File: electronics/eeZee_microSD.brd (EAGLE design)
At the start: 18.3 x 29.8 mm, 14 parts, among them U1 MCP1824S, U2 74HC4050, U3 USD-SOCKET

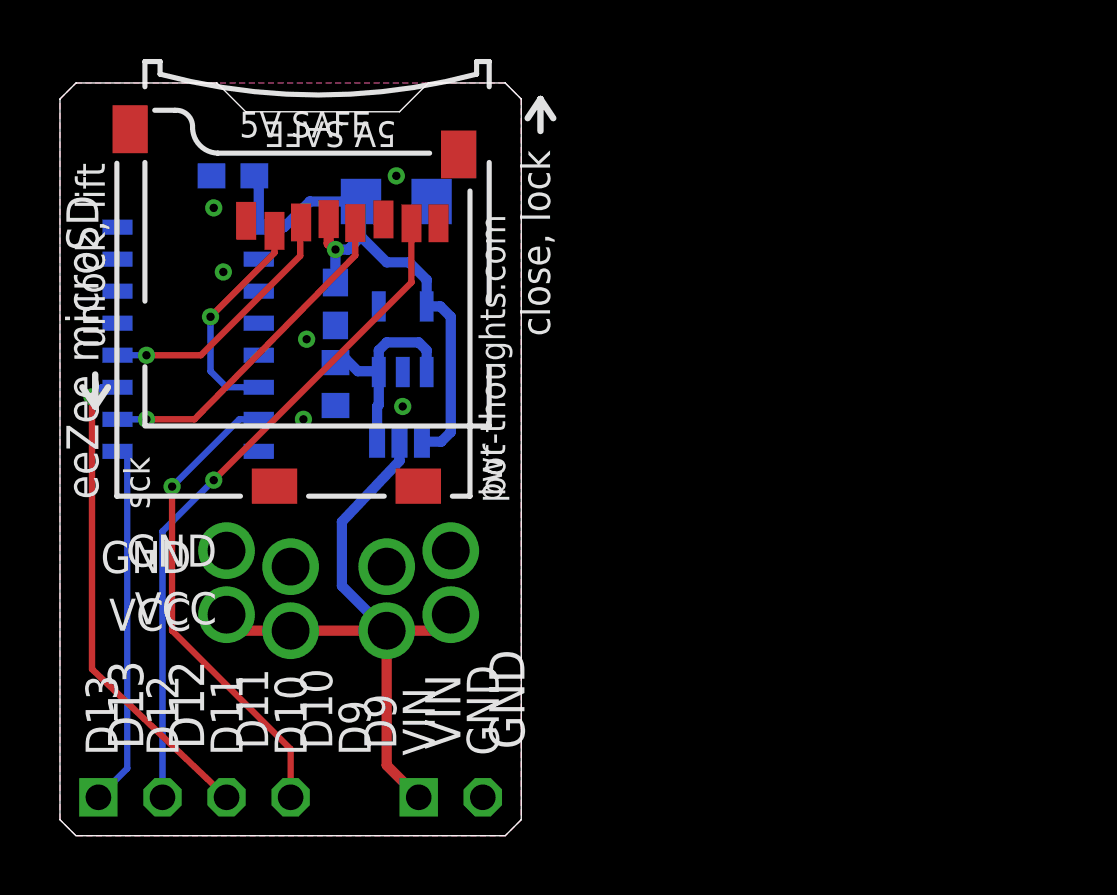
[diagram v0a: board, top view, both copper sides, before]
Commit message: modified silk layout
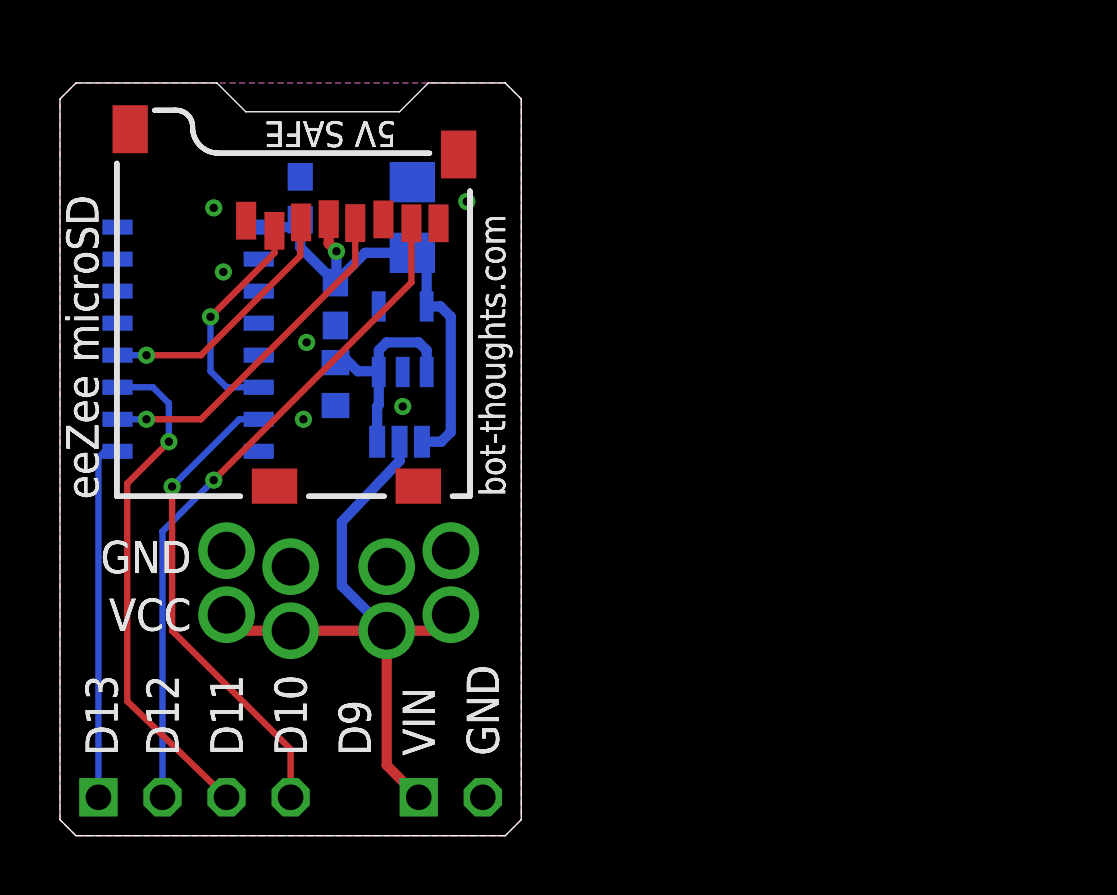
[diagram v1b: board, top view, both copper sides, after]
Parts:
- moved C2 2.81 mm to (9.53, 25.3), turned to 90 degrees
- moved C1 0.90 mm to (14.0, 24.5), turned to 90 degrees
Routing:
- net VCC: track 23.4 -> 20.4 mm
- net MOSI_HV: track 19.3 -> 20.3 mm
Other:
- board text added: "104"
- board text added: "106"
- board text added: "10K"
- board text added: "74HC4050"
- board text added: "MCP1824S"
- board text removed: "C1"
- board text removed: "C2"
- board text removed: "C3"
- board text removed: "R0.2"
- board text removed: "R5"
- board text removed: "U1"
- board text removed: "U2"
- board text removed: "close, lock"
- board text removed: "pwr"
- board text removed: "sck"
- board text removed: "unlock, lift"

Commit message: Updated schematic version and usd socket value
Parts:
- U3: value USD-SOCKET -> USD-PUSHPULL
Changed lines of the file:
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@@
 <attribute name="DATABASE" value="./../../../eagle/PARTSDB.TXT" x="12.954" y="8.128" size="1.778" layer="28" rot="MR90" display="off"/>
 </element>
-<element name="U3" library="SparkFun-Connectors" package="MICROSD_1:1" value="USD-SOCKET" x="2.286" y="13.462" smashed="yes">
+<element name="U3" library="SparkFun-Connectors" package="MICROSD_1:1" value="USD-PUSHPULL" x="2.286" y="13.462" smashed="yes">
 <attribute name="PROD_ID" value="CONN-07820" x="2.286" y="13.462" size="1.778" layer="27" display="off"/>
 </element>

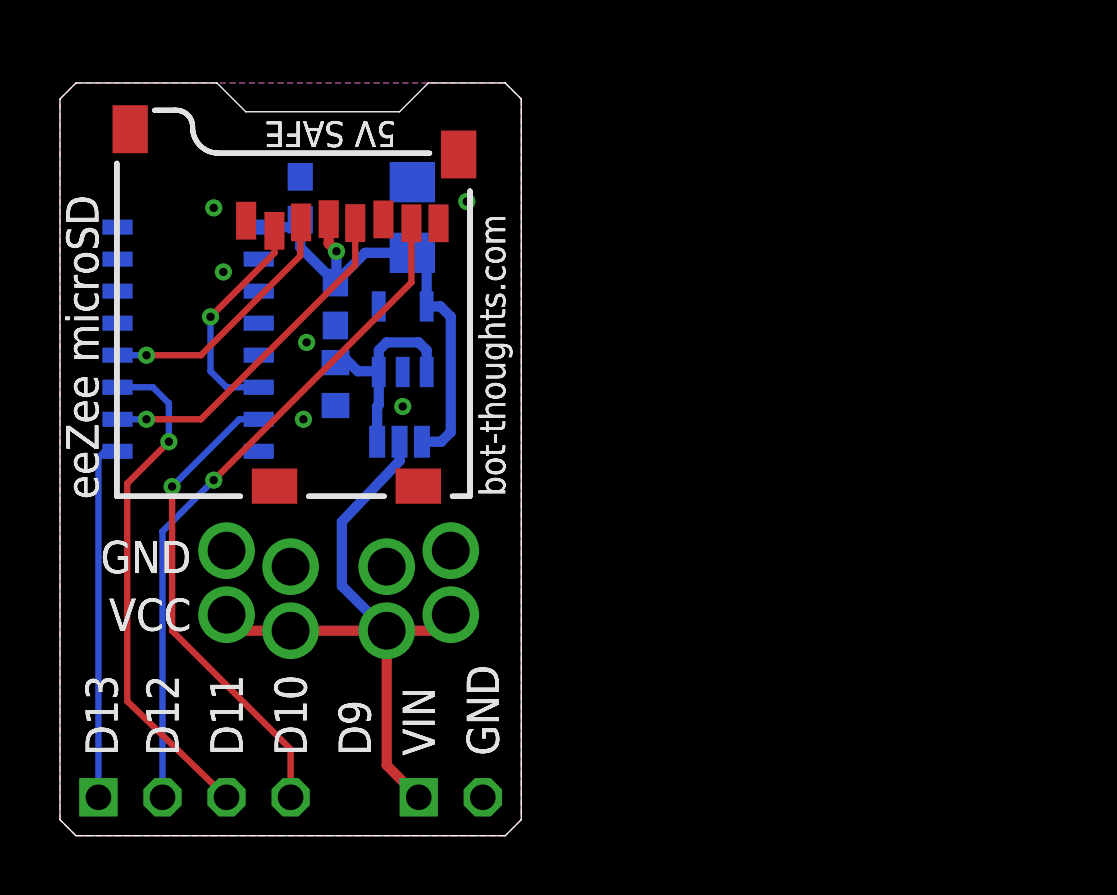
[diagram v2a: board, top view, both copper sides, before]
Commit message: Updated version with flip-top socket
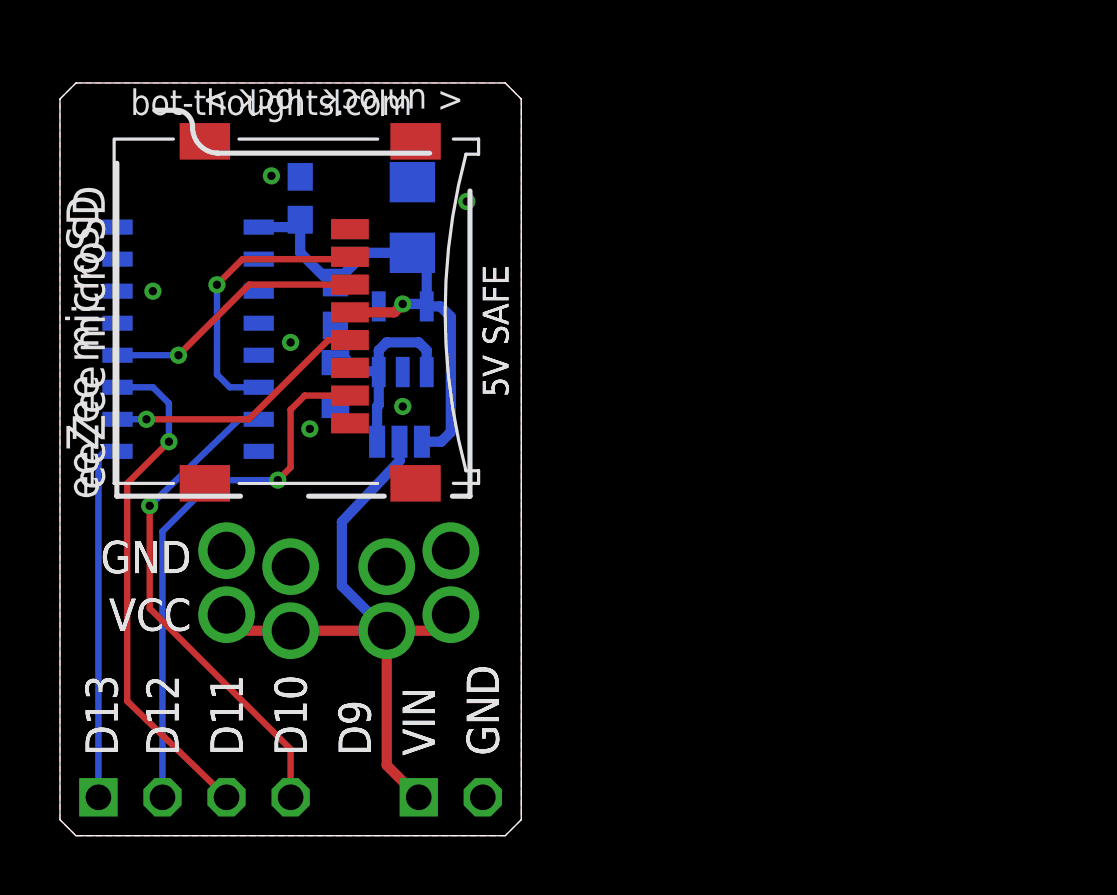
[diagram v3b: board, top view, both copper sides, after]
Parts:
- removed U3: USD-PUSHPULL, SparkFun-Connectors:MICROSD_1:1
- added U$1: MICROSD_TFLASH, bt_electromech:TFLASH_CP-0000-086
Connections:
- net !SS: now also U$1.CS; no longer U3.2
- net GND: now also U$1.GND, U$1.SHIELD1, U$1.SHIELD2, U$1.SHIELD3, U$1.SHIELD4; no longer U3.6, U3.CD1, U3.CD2, U3.GND1, U3.GND3
- net MISO: now also U$1.DO; no longer U3.7
- net MOSI: now also U$1.DI; no longer U3.3
- net SCK: now also U$1.SCLK; no longer U3.5
- net VCC: now also U$1.VDD; no longer U3.4
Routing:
- net MISO: track 26.8 -> 21.5 mm
- net SCK: track 13.6 -> 10.5 mm
- net !SS: track 8.79 -> 11.2 mm
- net !CS_HV: track 18.8 -> 19.6 mm
- net VCC: track 20.4 -> 21.1 mm
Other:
- outline, holes or cut-outs redrawn
- board text added: "< unlock lock >"
- board text added: "R0.3B"

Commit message: Used small manual connector. Total layout redesign, shrunk board considerably, removed power rail pin headers
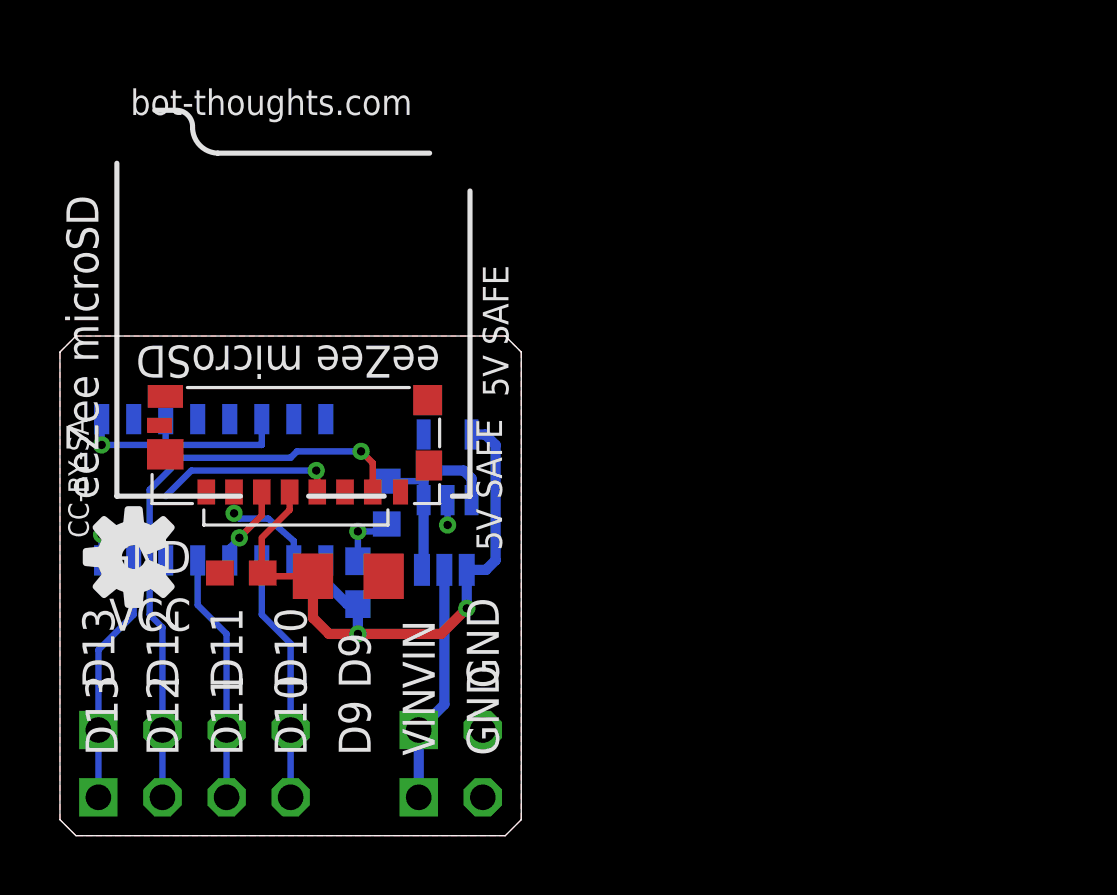
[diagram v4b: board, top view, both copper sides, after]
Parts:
- removed JP4, JP5: PWR, mes_electromech:BIGPIN-2
- removed U$1: MICROSD_TFLASH, bt_electromech:TFLASH_CP-0000-086
- added U3: MICROSD_SMALL, bt_electromech:USD_SMALL
- JP1: value (none) -> PWR
- JP2: value PWR -> (none); device mes_electromech:BIGPIN-2 -> pinhead-2:1X04-S
- JP3: device mes_electromech:BIGPIN-2 -> pinhead-2:1X02-S
- moved C2 15.4 mm to (11.8, 10.0)
- moved C1 14.4 mm to (11.4, 10.3), flipped to the top, turned to 0 degrees
- moved JP2 12.5 mm to (5.33, 1.52), turned to 180 degrees
- moved C3 11.3 mm to (7.19, 10.4), flipped to the top, turned to 180 degrees
- moved JP3 9.16 mm to (15.5, 1.52), turned to 180 degrees
- moved U2 6.05 mm to (6.10, 13.7), turned to 0 degrees
- moved REG 5.38 mm to (15.2, 10.5)
- moved U1 5.38 mm to (15.4, 14.6)
- moved R5 5.12 mm to (13.0, 13.2)
- moved JP1 2.67 mm to (15.5, 4.19)
- moved JP6 2.67 mm to (5.33, 4.19)
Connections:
- removed net VBOARD: JP1.1, JP2.P$1, JP3.P$1, JP4.P$1, JP5.P$1, REG.2
- new net VIN: JP1.1, JP3.1, REG.2
- net !CS_HV: now also JP2.4, U2.3; no longer U2.7
- net !SS: now also U2.2, U3.2; no longer U$1.CS, U2.6
- net GND: now also JP3.2, U2.11, U2.9, U3.6, U3.GND1, U3.GND2, U3.GND3, U3.GND4; no longer JP2.P$2, JP3.P$2, JP4.P$2, JP5.P$2, U$1.GND, U$1.SHIELD1, U$1.SHIELD2, U$1.SHIELD3, U$1.SHIELD4, U2.3, U2.5
- net MISO: now also JP2.2, U3.7; no longer U$1.DO
- net MOSI: now also U2.4, U3.3; no longer U$1.DI, U2.12
- net MOSI_HV: now also JP2.3, U2.5; no longer U2.11
- net SCK: now also U2.6, U3.5; no longer U$1.SCLK, U2.10
- net SCK_HV: now also JP2.1, U2.7; no longer U2.9
- net VCC: now also U3.4; no longer U$1.VDD
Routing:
- net VBOARD: track 25.7 -> 0.00 mm
- net GND: track 0.00 -> 13.9 mm, vias 6 -> 4
- net MOSI_HV: track 20.3 -> 10.0 mm, vias 1 -> 0
- net !CS_HV: track 19.6 -> 9.87 mm, vias 1 -> 0
- net VIN: track 0.00 -> 9.44 mm
- net !SS: track 11.2 -> 3.56 mm
- net MOSI: track 10.4 -> 3.24 mm
- net VCC: track 21.1 -> 26.4 mm, vias 1 -> 2
- net SCK_HV: track 14.7 -> 9.97 mm
- net SCK: track 10.5 -> 7.26 mm
- net MISO: track 21.5 -> 23.2 mm
- removed copper zone on layer 16, net GND
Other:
- board size 18.3 x 29.8 mm -> 18.3 x 19.8 mm
- board text removed: "< unlock lock >"

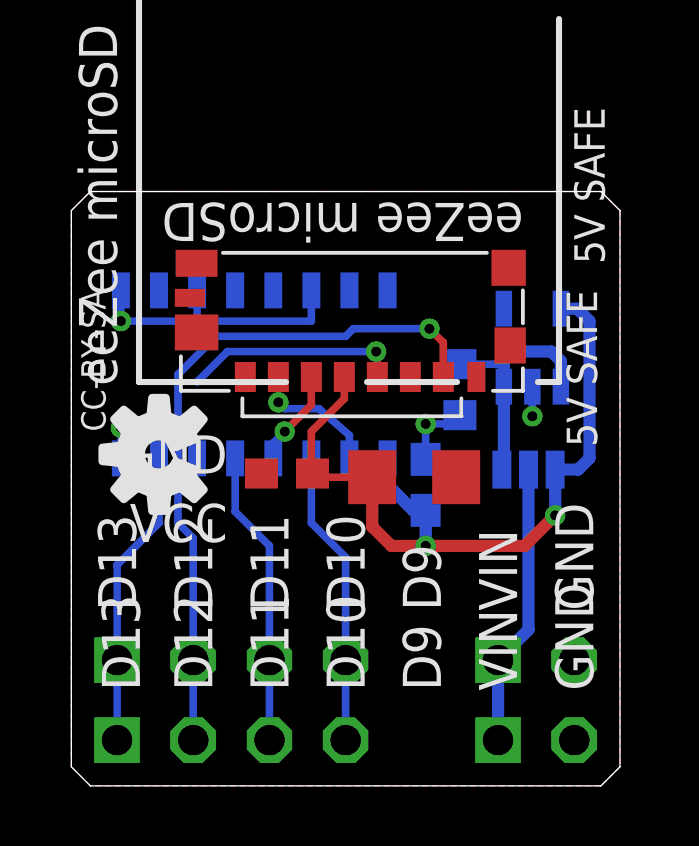
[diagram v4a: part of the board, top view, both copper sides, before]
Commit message: Additional layout changes, connected Card Detect
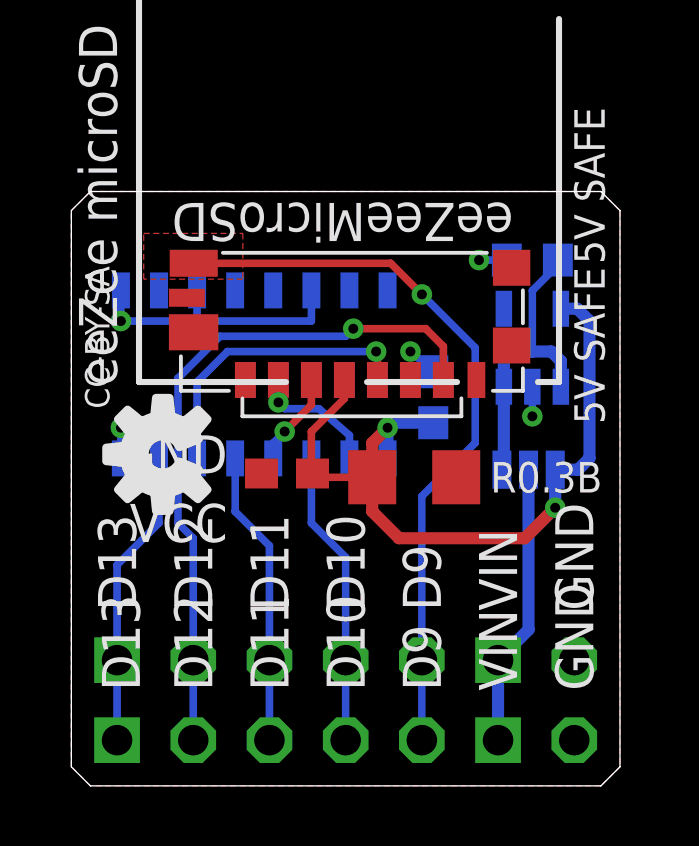
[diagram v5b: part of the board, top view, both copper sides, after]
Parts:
- removed JP6: (no value), pinhead-2:1X04-S
- added JP4: (no value), pinhead-2:1X05-S
- JP2: value (none) -> PWR; device pinhead-2:1X04-S -> pinhead-2:1X02-S
- JP3: value PWR -> (none); device pinhead-2:1X02-S -> pinhead-2:1X05-S
- U4: value MICROSD_SMALL -> MICROSD_CD
- moved JP2 10.2 mm to (15.5, 1.52)
- moved JP3 8.89 mm to (6.60, 1.52)
- moved R5 4.95 mm to (15.4, 17.5), turned to 180 degrees
- moved C2 2.93 mm to (12.1, 13.0)
- renumbered U3 to U4
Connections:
- new net CD: JP3.5, JP4.5, U4.DET
- net !CS_HV: now also JP3.4, JP4.4; no longer JP2.4, JP6.4
- net GND: now also JP2.2, U4.POL; no longer JP3.2, U4.GND2
- net MISO: now also JP3.2, JP4.2; no longer JP2.2, JP6.2
- net MOSI_HV: now also JP3.3, JP4.3; no longer JP2.3, JP6.3
- net SCK_HV: now also JP3.1, JP4.1; no longer JP2.1, JP6.1
- net VIN: now also JP2.1; no longer JP3.1
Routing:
- net CD: track 0.00 -> 24.4 mm, vias 0 -> 1
- net SCK: track 7.26 -> 9.90 mm
- net VREGIN: track 8.18 -> 10.1 mm
- net !SS: track 3.56 -> 4.30 mm
- net GND: track 13.9 -> 13.4 mm, vias 4 -> 5
- added copper zone on layer 1, net CD
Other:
- board text added: "!DET"
- board text added: "eeZeeMicroSD"

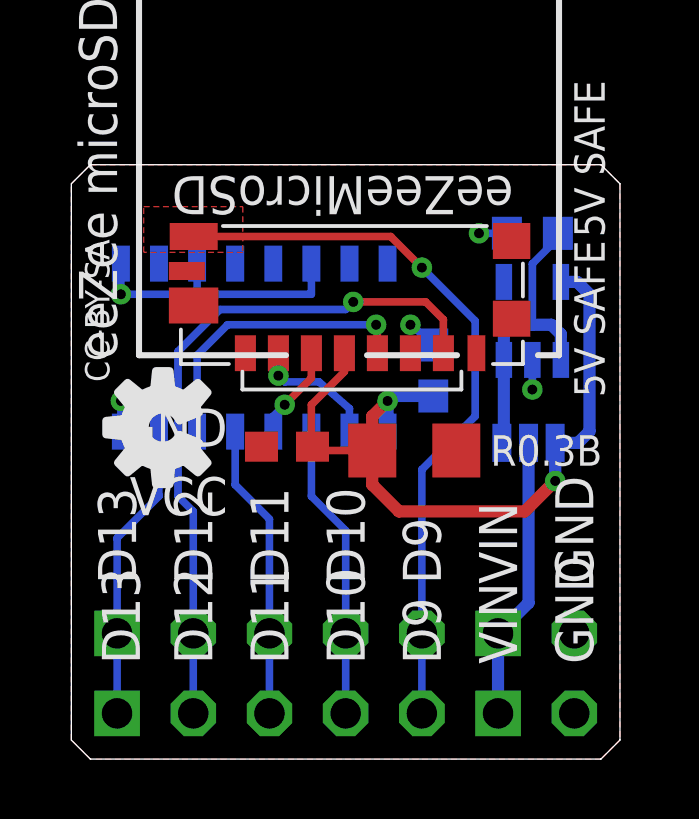
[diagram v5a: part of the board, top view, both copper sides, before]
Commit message: new regulator
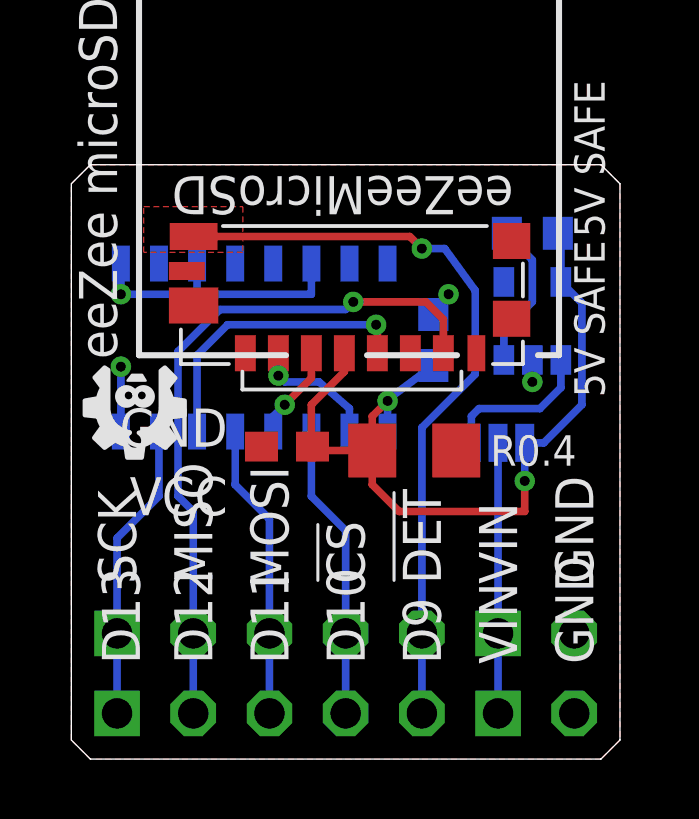
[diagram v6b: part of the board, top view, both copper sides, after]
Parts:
- removed REG: BYP, SparkFun:SJ_3
- added 5V: 3.3V, SparkFun:SJ_3
- added U$5: BTLOGO-LOGO-SM, bt:BTLOGOS
- U1: value MCP1824S -> MIC5317; device mes_regulators:SOT23-5 -> bt_regulator:SOT23-5
- moved C2 1.02 mm to (12.1, 14.0)
- turned R5 to 0 degrees
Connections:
- new net EN: R5.2, U1.3
- net GND: no longer R5.1
- net VCC: now also 5V.1, R5.1; no longer REG.1
- net VIN: now also 5V.2; no longer REG.2
- net VREGIN: now also 5V.3; no longer R5.2, REG.3, U1.3
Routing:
- net EN: track 0.00 -> 4.97 mm
- net VREGIN: track 10.1 -> 5.19 mm
- net VCC: track 26.4 -> 27.8 mm
- net CD: track 24.4 -> 25.1 mm
- net GND: track 13.4 -> 13.3 mm, vias 5 -> 4
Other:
- board text added: "R0.4"
- board text added: "VIN="
- board text removed: "R0.3B"

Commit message: rotated board
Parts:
- moved R5 14.8 mm to (17.5, 2.92), turned to 90 degrees
- moved JP2 14.0 mm to (1.52, 2.79), turned to 270 degrees
- moved U1 11.7 mm to (14.6, 2.92), turned to 90 degrees
- moved U$5 11.4 mm to (13.2, 16.1), turned to 90 degrees
- moved JP1 11.4 mm to (4.19, 2.79), turned to 270 degrees
- moved JP3 11.4 mm to (1.52, 11.7), turned to 270 degrees
- moved C2 7.98 mm to (14.0, 6.22), turned to 180 degrees
- moved JP4 7.87 mm to (4.19, 11.7), turned to 270 degrees
- moved U2 7.77 mm to (13.7, 12.2), turned to 90 degrees
- moved 5V 7.45 mm to (10.5, 4.06), turned to 90 degrees
- moved U4 4.55 mm to (12.3, 8.64), turned to 90 degrees
- moved C1 3.61 mm to (10.3, 6.86), turned to 270 degrees
- moved C3 3.30 mm to (10.4, 11.1), turned to 90 degrees
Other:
- board size 18.3 x 19.8 mm -> 19.8 x 18.3 mm
